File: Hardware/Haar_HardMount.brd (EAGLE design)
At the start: 29.1 x 10.1 mm, 15 parts, among them J1 CONN_42.54, Q1 2N7002, U1 SHT35DFN, U2 LPS35HW, U4 TPS62237DRY, U5 TXS0102DQM

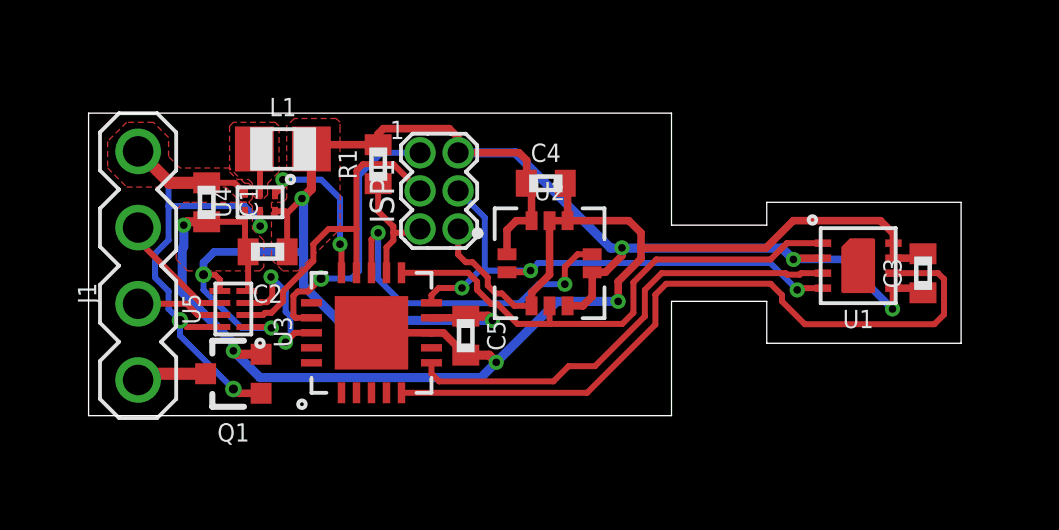
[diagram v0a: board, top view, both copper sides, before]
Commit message: Added HardMount version, improved layout on conventional version
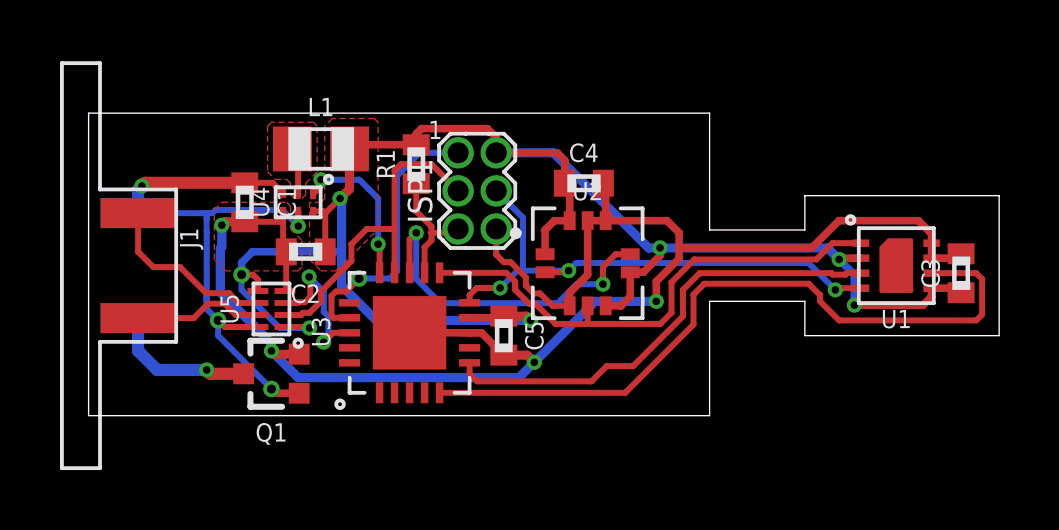
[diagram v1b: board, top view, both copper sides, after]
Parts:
- J1: value CONN_42.54 -> SOLDERCUP_CONN_QUAD; device bschulz:1X04 -> bschulz:SOLDERCUP_CONN_QUAD
- moved C4 1.27 mm to (16.5, 7.75)
- moved ISP1 1.27 mm to (13.0, 7.49)
- moved R1 1.27 mm to (10.9, 8.38)
- moved Q1 1.27 mm to (6.10, 1.40)
- moved U4 1.27 mm to (6.99, 7.11)
- moved U5 1.27 mm to (6.10, 3.56)
- moved C1 1.27 mm to (5.21, 7.11)
- moved J1 1.27 mm to (0.38, 5.00), turned to 270 degrees
- moved C2 1.27 mm to (7.24, 5.46)
- moved C3 1.27 mm to (29.1, 4.75)
- moved C5 1.27 mm to (13.8, 2.67)
- moved L1 1.27 mm to (7.75, 8.89)
- moved U1 1.27 mm to (26.9, 5.00)
- moved U2 1.27 mm to (16.6, 5.08)
- moved U3 1.27 mm to (10.7, 2.79)
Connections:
- net SCL_EXT_HV: now also J1.1; no longer J1.2
- net SDA_EXT_HV: now also J1.2; no longer J1.3
- net VIN+: now also J1.3; no longer J1.4
- net VIN-: now also J1.4; no longer J1.1
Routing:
- net VIN-: track 2.34 -> 4.93 mm, vias 0 -> 1
- net SDA_EXT_HV: track 4.23 -> 6.20 mm
- net SCL_EXT_HV: track 2.88 -> 4.35 mm
- net VIN+: track 20.1 -> 21.5 mm, vias 3 -> 4
- removed copper zone on layer 1, net VIN+
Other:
- board size 29.1 x 10.1 mm -> 30.4 x 10.1 mm

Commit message: Fixed ISP error, updated notes
Fixed an errant connection to the ISP header on both versions in schematic, still need to fix the layout. Also removed outdated notes on schematic
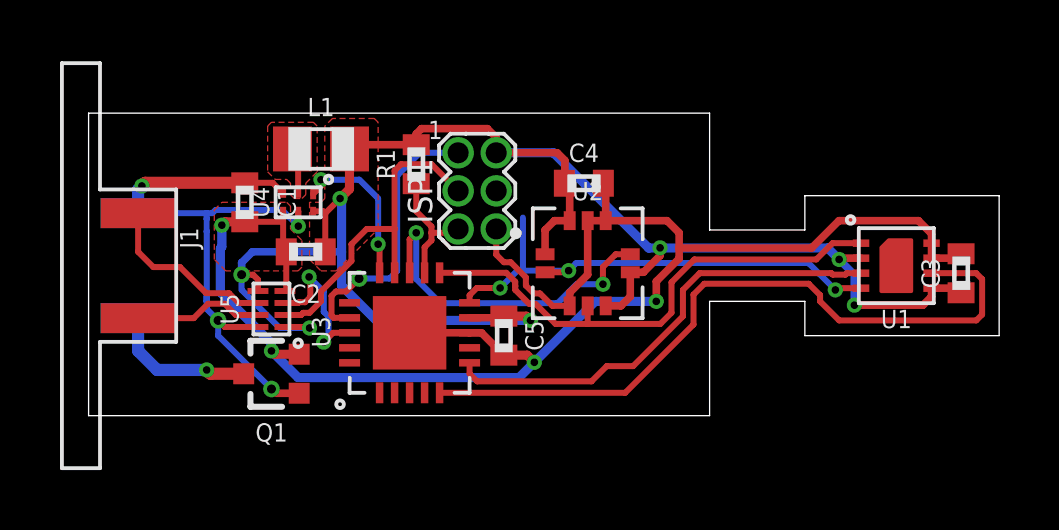
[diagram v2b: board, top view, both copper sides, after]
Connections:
- net SCL: no longer ISP1.4
- net SDA_EXT: now also ISP1.4
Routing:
- net SCL: track 18.0 -> 16.7 mm
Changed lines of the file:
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@@
 <wire x1="8.001" y1="3.302" x2="8.001" y2="2.6127375" width="0.2" layer="16"/>
 <wire x1="8.001" y1="2.6127375" x2="7.83763125" y2="2.44936875" width="0.2" layer="16"/>
+<contactref element="ISP1" pad="4"/>
+<wire x1="7.83763125" y1="4.13731875" x2="13.589" y2="7.493" width="0" layer="19" extent="16-16"/>
 </signal>
 <signal name="RX">
@@
 <contactref element="U1" pad="4"/>
 <contactref element="U2" pad="2"/>
-<contactref element="ISP1" pad="4"/>
 <wire x1="12.9396" y1="4.2556" x2="12.7" y2="4.016" width="0.2" layer="1"/>
 <wire x1="12.7" y1="3.762" x2="12.7" y2="4.016" width="0.2" layer="1"/>
@@
 <wire x1="24.892" y1="4.191" x2="24.951" y2="4.25" width="0.2" layer="1"/>
 <wire x1="24.951" y1="4.25" x2="25.749" y2="4.25" width="0.2" layer="1"/>
-<wire x1="13.589" y1="7.493" x2="14.478" y2="6.604" width="0.2" layer="16"/>
 <wire x1="14.478" y1="6.604" x2="14.478" y2="4.834" width="0.2" layer="16"/>
 </signal>

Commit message: Reroute; dimensions
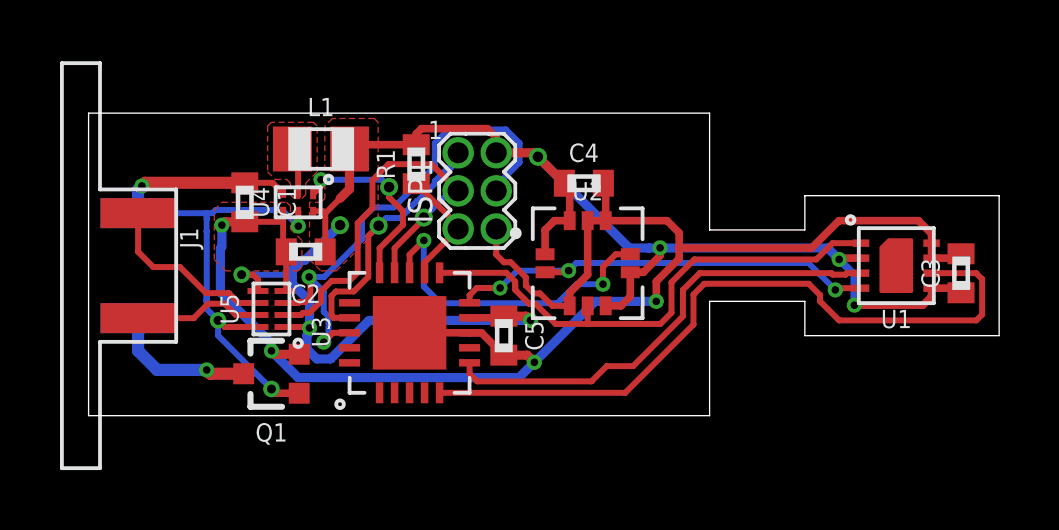
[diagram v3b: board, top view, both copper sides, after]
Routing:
- net SDA_EXT: track 5.18 -> 17.2 mm
- net 3V3: track 60.2 -> 56.3 mm, vias 7 -> 8
- net SCL_EXT: track 11.3 -> 13.7 mm, vias 0 -> 1
- net SCL: track 16.7 -> 15.0 mm
- net BUCK_MODE: track 5.25 -> 6.33 mm
- net MISO: track 9.35 -> 8.50 mm
- net PRES_INT: track 11.4 -> 10.9 mm

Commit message: Fixed routing, cleaned up, ready for fab
Minor routing fixes, added some silkscreen, generated gerbers, ready for prototype fab
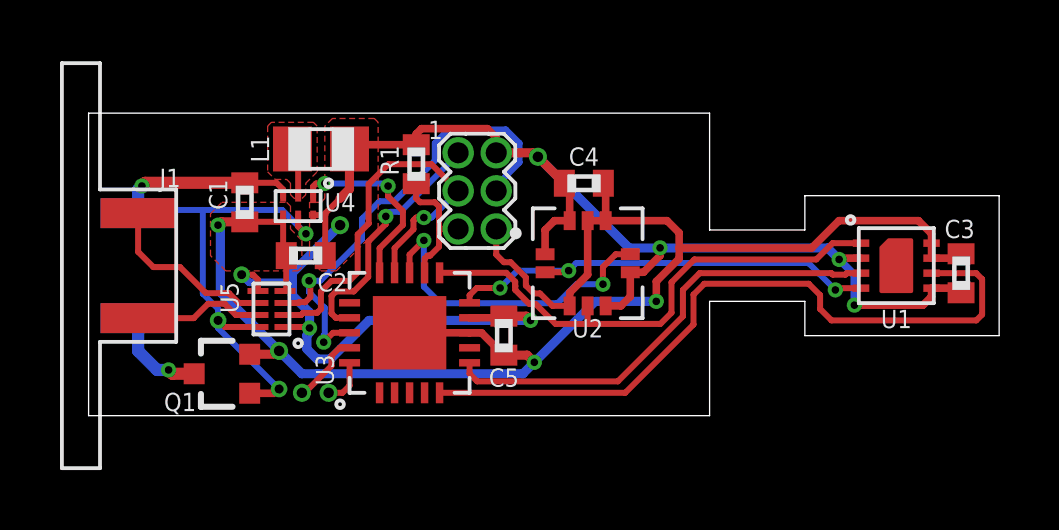
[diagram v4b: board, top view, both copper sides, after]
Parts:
- moved Q1 1.65 mm to (4.45, 1.40)
- moved C2 0.13 mm to (7.24, 5.33)
- moved U4 0.13 mm to (6.99, 6.99)
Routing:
- net TX: track 0.00 -> 2.41 mm, vias 0 -> 1
- net VIN-: track 4.93 -> 3.28 mm
- net RX: track 0.00 -> 1.56 mm, vias 0 -> 1
- net VIN+: track 21.5 -> 22.2 mm
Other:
- board text added: "Project Haar v0.0 ---------------- Developed by Northern Widget and University of Minnesota"

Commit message: Minor dimensional cleanup, final gerbers generated
Fixed dimensional alignment, generated gerbers, sent to fab
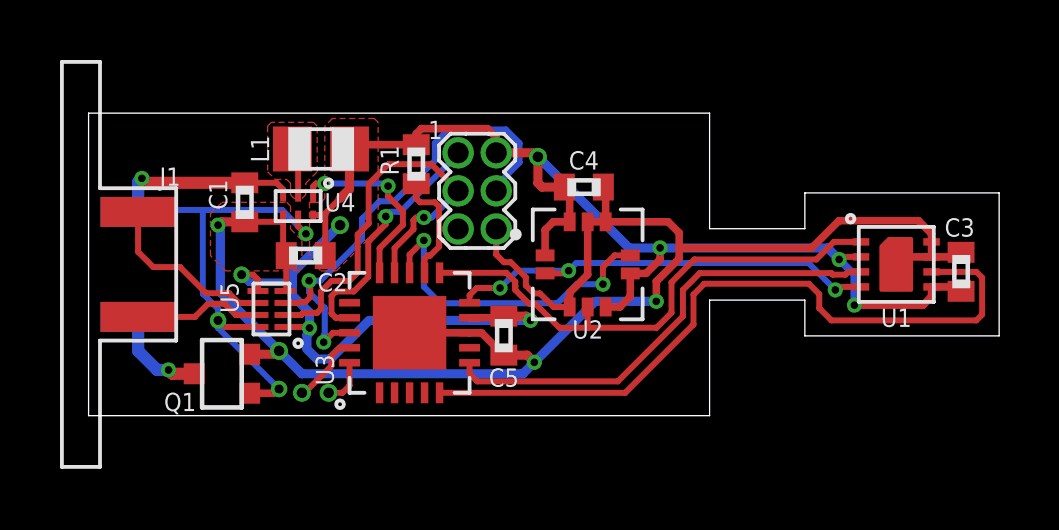
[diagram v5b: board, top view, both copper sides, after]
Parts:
- moved C4 0.13 mm to (16.5, 7.62)
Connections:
- net GND: now also U1.EP
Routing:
- net GND: track 54.5 -> 56.3 mm
- net 3V3: track 56.4 -> 57.4 mm
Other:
- outline, holes or cut-outs redrawn

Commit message: Updated part values, added prelim firmware
Added values to parts for full BoM generation, added preliminary test firmware, consolidation and streamlining to come, simply proof of functionality at the moment
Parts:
- C3, C4, C5: value (none) -> 0.1uF
- L1: value (none) -> 2.2uH
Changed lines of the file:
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@@
 <grid distance="50" unitdist="mil" unit="mm" style="lines" multiple="1" display="no" altdistance="5" altunitdist="mil" altunit="mm"/>
 <layers>
-<layer number="1" name="Top" color="4" fill="1" visible="yes" active="yes"/>
+<layer number="1" name="Top" color="4" fill="1" visible="no" active="yes"/>
 <layer number="2" name="Route2" color="16" fill="1" visible="no" active="no"/>
 <layer number="3" name="Route3" color="17" fill="1" visible="no" active="no"/>
@@
 <layer number="16" name="Bottom" color="1" fill="1" visible="no" active="yes"/>
 <layer number="17" name="Pads" color="2" fill="1" visible="yes" active="yes"/>
-<layer number="18" name="Vias" color="2" fill="1" visible="yes" active="yes"/>
+<layer number="18" name="Vias" color="2" fill="1" visible="no" active="yes"/>
 <layer number="19" name="Unrouted" color="6" fill="1" visible="yes" active="yes"/>
 <layer number="20" name="Dimension" color="24" fill="1" visible="yes" active="yes"/>
-<layer number="21" name="tPlace" color="7" fill="1" visible="no" active="yes"/>
+<layer number="21" name="tPlace" color="7" fill="1" visible="yes" active="yes"/>
 <layer number="22" name="bPlace" color="7" fill="1" visible="no" active="yes"/>
 <layer number="23" name="tOrigins" color="15" fill="1" visible="yes" active="yes"/>
 <layer number="24" name="bOrigins" color="15" fill="1" visible="no" active="yes"/>
-<layer number="25" name="tNames" color="7" fill="1" visible="no" active="yes"/>
+<layer number="25" name="tNames" color="7" fill="1" visible="yes" active="yes"/>
 <layer number="26" name="bNames" color="7" fill="1" visible="no" active="yes"/>
 <layer number="27" name="tValues" color="7" fill="1" visible="no" active="yes"/>
@@
 <layer number="29" name="tStop" color="7" fill="3" visible="no" active="yes"/>
 <layer number="30" name="bStop" color="7" fill="6" visible="no" active="yes"/>
-<layer number="31" name="tCream" color="7" fill="4" visible="yes" active="yes"/>
+<layer number="31" name="tCream" color="7" fill="4" visible="no" active="yes"/>
 <layer number="32" name="bCream" color="7" fill="5" visible="no" active="yes"/>
 <layer number="33" name="tFinish" color="6" fill="3" visible="no" active="yes"/>
@@
 <attribute name="VALUE" x="7.239" y="6.731" size="0.6096" layer="27" font="vector" ratio="15" rot="R180" align="center"/>
 </element>
-<element name="C3" library="bschulz_passives" package="C0402" value="" x="29.083" y="4.796" smashed="yes" rot="R90">
+<element name="C3" library="bschulz_passives" package="C0402" value="0.1uF" x="29.083" y="4.796" smashed="yes" rot="R90">
 <attribute name="DIGIKEY" value="490-4759-1-ND" x="53.213" y="21.306" size="1.778" layer="27" rot="R90" display="off"/>
 <attribute name="MF" value="Murata" x="53.213" y="21.306" size="1.778" layer="27" rot="R90" display="off"/>
@@
 <attribute name="VALUE" x="30.099" y="4.796" size="0.6096" layer="27" font="vector" ratio="15" rot="R90" align="center"/>
 </element>
-<element name="C4" library="bschulz_passives" package="C0402" value="" x="16.51" y="7.62" smashed="yes">
+<element name="C4" library="bschulz_passives" package="C0402" value="0.1uF" x="16.51" y="7.62" smashed="yes">
 <attribute name="DIGIKEY" value="490-4759-1-ND" x="36.83" y="-16.51" size="1.778" layer="27" display="off"/>
 <attribute name="MF" value="Murata" x="36.83" y="-16.51" size="1.778" layer="27" display="off"/>
@@
 <attribute name="VALUE" x="16.51" y="6.604" size="0.6096" layer="27" font="vector" ratio="15" align="center"/>
 </element>
-<element name="C5" library="bschulz_passives" package="C0402" value="" x="13.843" y="2.667" smashed="yes" rot="R270">
+<element name="C5" library="bschulz_passives" package="C0402" value="0.1uF" x="13.843" y="2.667" smashed="yes" rot="R270">
 <attribute name="DIGIKEY" value="490-4759-1-ND" x="-10.287" y="-21.463" size="1.778" layer="27" rot="R270" display="off"/>
 <attribute name="MF" value="Murata" x="-10.287" y="-21.463" size="1.778" layer="27" rot="R270" display="off"/>
@@
 <attribute name="VALUE" x="-1.651" y="6.312" size="0.6096" layer="27" font="vector" ratio="20" rot="R270"/>
 </element>
-<element name="L1" library="bschulz" package="0805" value="" x="7.747" y="8.89" smashed="yes">
+<element name="L1" library="bschulz" package="0805" value="2.2uH" x="7.747" y="8.89" smashed="yes">
 <attribute name="NAME" x="5.715" y="8.89" size="0.6096" layer="25" font="vector" ratio="15" rot="R90" align="center"/>
 <attribute name="VALUE" x="7.747" y="7.493" size="0.6096" layer="27" font="vector" ratio="15" align="center"/>
